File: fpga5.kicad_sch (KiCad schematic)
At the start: 4 parts, among them P1 5CEFA7F23

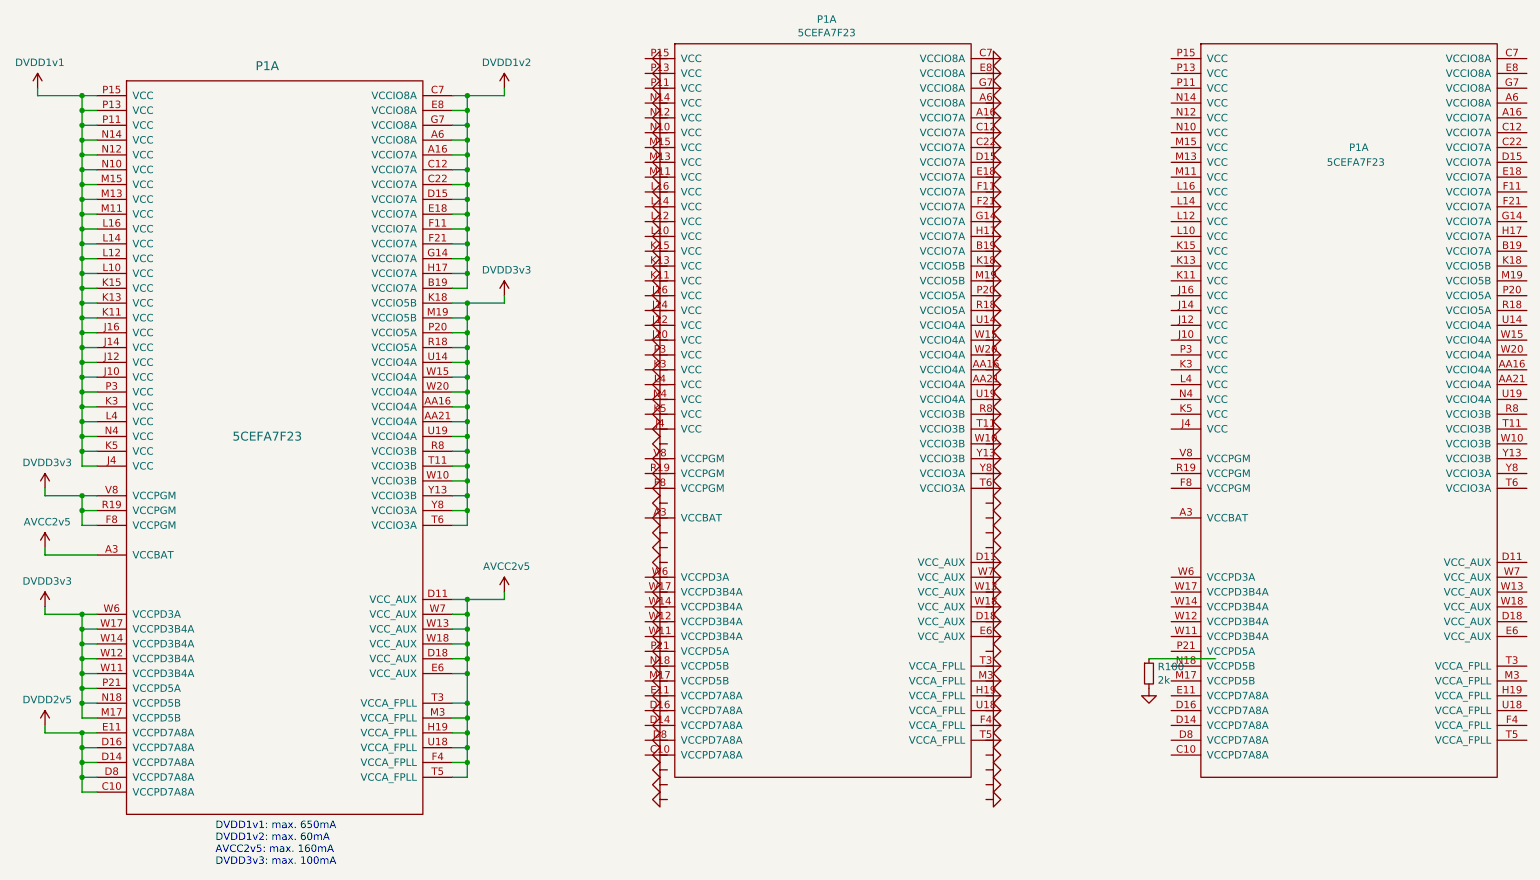
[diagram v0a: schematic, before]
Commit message: update schematic to v1.5
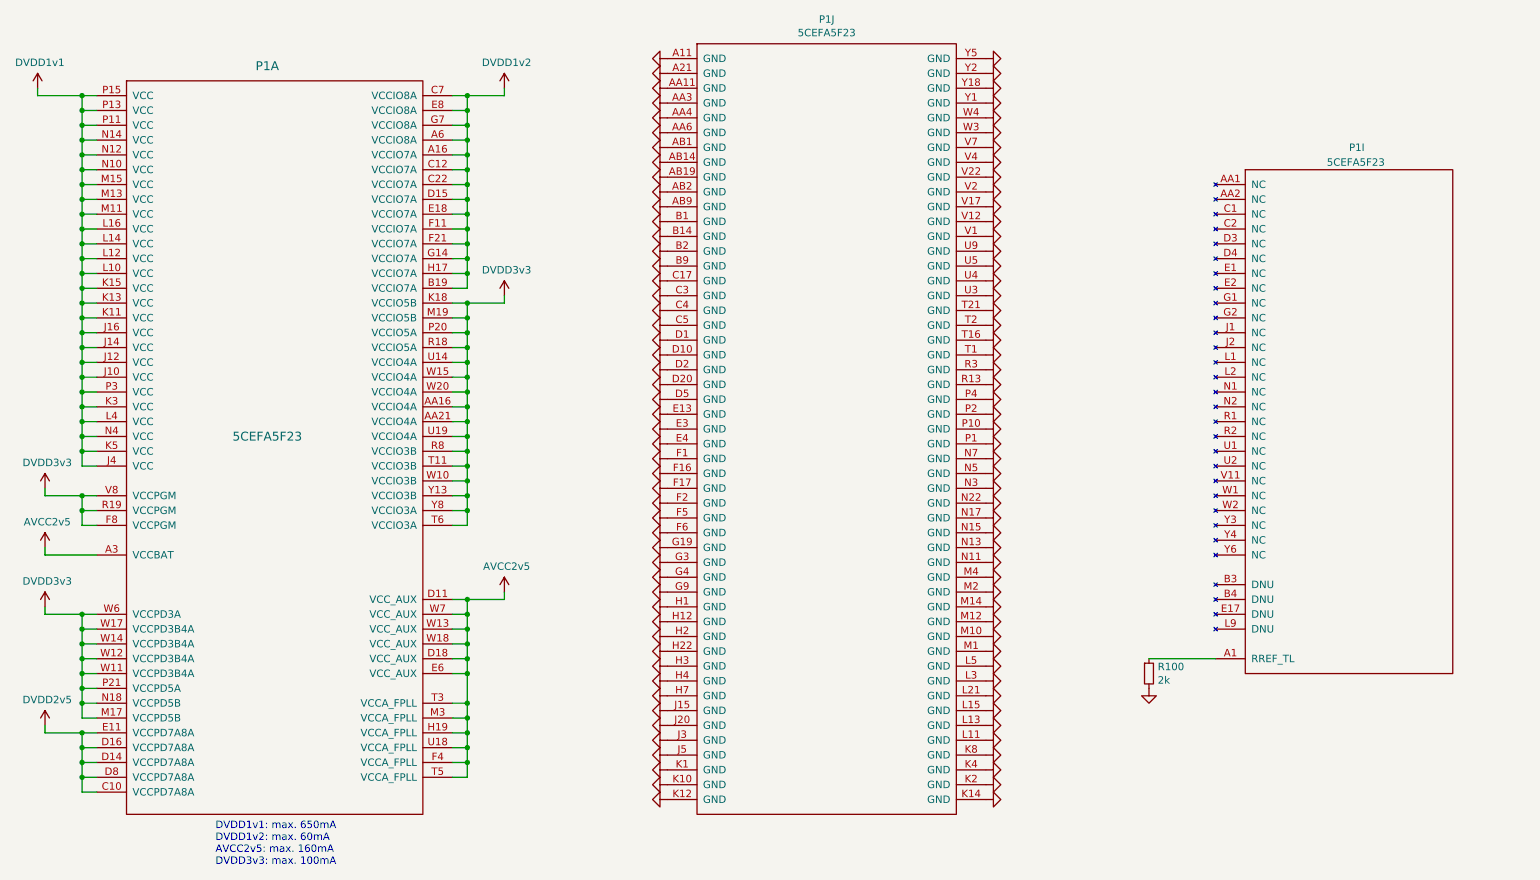
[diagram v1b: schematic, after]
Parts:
- P1: value 5CEFA7F23 -> 5CEFA5F23
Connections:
- net GND: now also P1.A11 (GND), P1.A21 (GND), P1.AA11 (GND), P1.AA3 (GND), P1.AA4 (GND), P1.AA6 (GND), P1.AB1 (GND), P1.AB14 (GND), P1.AB19 (GND), P1.AB2 (GND), P1.AB9 (GND), P1.B1 (GND), P1.B14 (GND), P1.B2 (GND), P1.B9 (GND), P1.C17 (GND), P1.C3 (GND), P1.C4 (GND), P1.C5 (GND), P1.D1 (GND), P1.D10 (GND), P1.D2 (GND), P1.D20 (GND), P1.D5 (GND), P1.E13 (GND), P1.E3 (GND), P1.E4 (GND), P1.F1 (GND), P1.F16 (GND), P1.F17 (GND), P1.F2 (GND), P1.F5 (GND), P1.F6 (GND), P1.G19 (GND), P1.G3 (GND), P1.G4 (GND), P1.G9 (GND), P1.H1 (GND), P1.H12 (GND), P1.H2 (GND), P1.H22 (GND), P1.H3 (GND), P1.H4 (GND), P1.H7 (GND), P1.J15 (GND), P1.J20 (GND), P1.J3 (GND), P1.J5 (GND), P1.K1 (GND), P1.K10 (GND), P1.K12 (GND), P1.K14 (GND), P1.K2 (GND), P1.K4 (GND), P1.K8 (GND), P1.L11 (GND), P1.L13 (GND), P1.L15 (GND), P1.L21 (GND), P1.L3 (GND), P1.L5 (GND), P1.M1 (GND), P1.M10 (GND), P1.M12 (GND), P1.M14 (GND), P1.M2 (GND), P1.M4 (GND), P1.N11 (GND), P1.N13 (GND), P1.N15 (GND), P1.N17 (GND), P1.N22 (GND), P1.N3 (GND), P1.N5 (GND), P1.N7 (GND), P1.P1 (GND), P1.P10 (GND), P1.P2 (GND), P1.P4 (GND), P1.R13 (GND), P1.R3 (GND), P1.T1 (GND), P1.T16 (GND), P1.T2 (GND), P1.T21 (GND), P1.U3 (GND), P1.U4 (GND), P1.U5 (GND), P1.U9 (GND), P1.V1 (GND), P1.V12 (GND), P1.V17 (GND), P1.V2 (GND), P1.V22 (GND), P1.V4 (GND), P1.V7 (GND), P1.W3 (GND), P1.W4 (GND), P1.Y1 (GND), P1.Y18 (GND), P1.Y2 (GND), P1.Y5 (GND)
- net at R100.1: now also P1.A1 (RREF_TL)
